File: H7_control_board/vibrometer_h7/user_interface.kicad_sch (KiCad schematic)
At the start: 26 parts, among them J501 Conn_02x08_Odd_Even, J502 Conn_02x08_Odd_Even, SW501 SW_Push, SW502 SW_Push

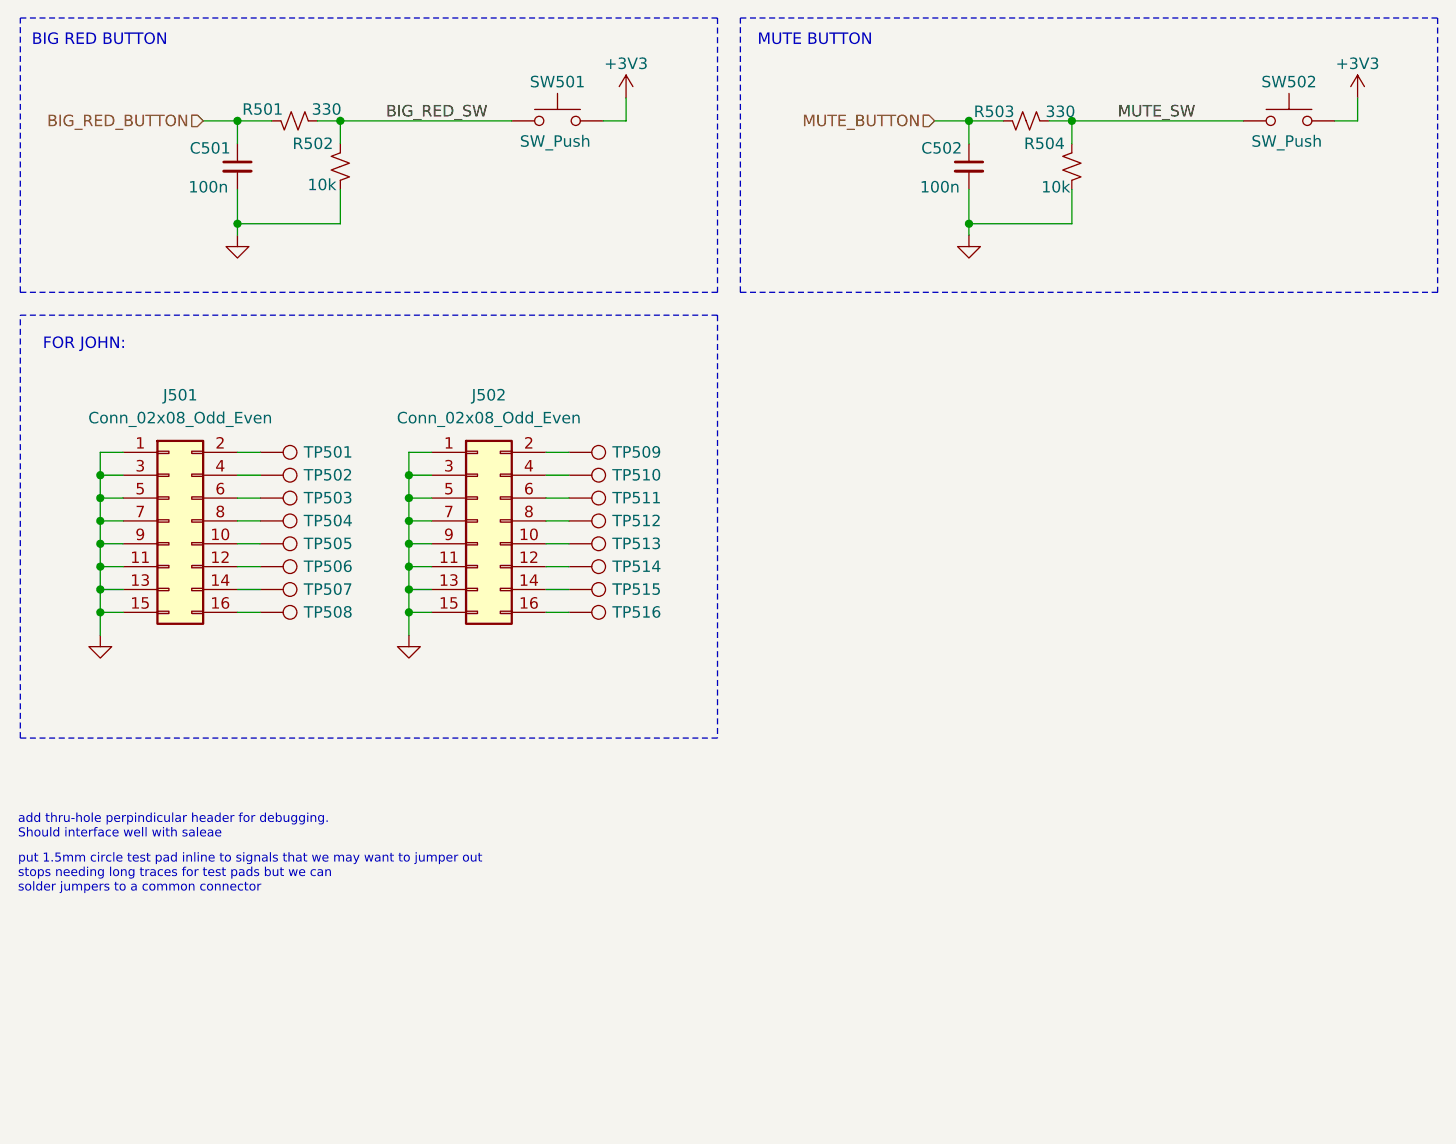
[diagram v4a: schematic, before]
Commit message: added indicator leds
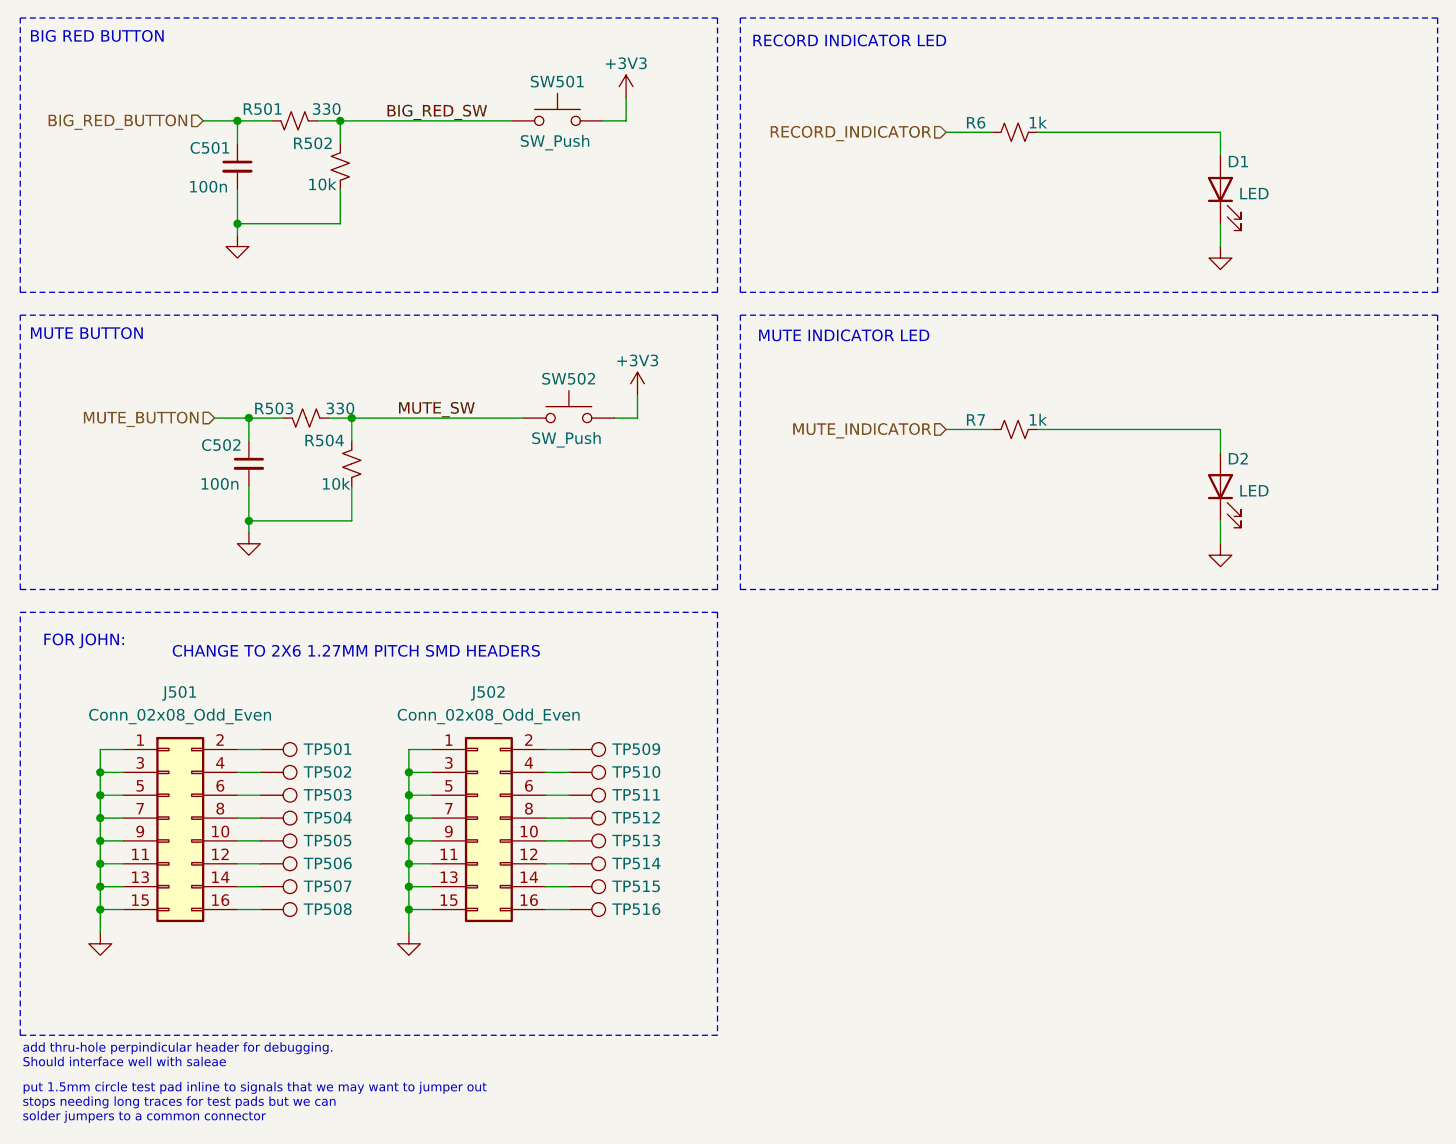
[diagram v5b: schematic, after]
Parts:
- added D1, D2: LED, LED_SMD:LED_0603_1608Metric, symbol Device:LED
- added R6, R7: 1k, Resistor_SMD:R_0603_1608Metric, symbol Device:R_Small_US
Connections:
- net GND: now also D1.1 (K), D2.1 (K)
- new net: D1.2 (A), R6.2
- new net: D2.2 (A), R7.2
- new net MUTE_INDICATOR: R7.1
- new net RECORD_INDICATOR: R6.1
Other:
- note added: "CHANGE TO 2X6 1.27MM PITCH SMD HEADERS"
- note added: "MUTE INDICATOR LED"
- note added: "RECORD INDICATOR LED"
- moved on the sheet: J501, J502, TP501, TP502, TP503, TP504, TP505, TP506, TP507, TP508, TP509, TP510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

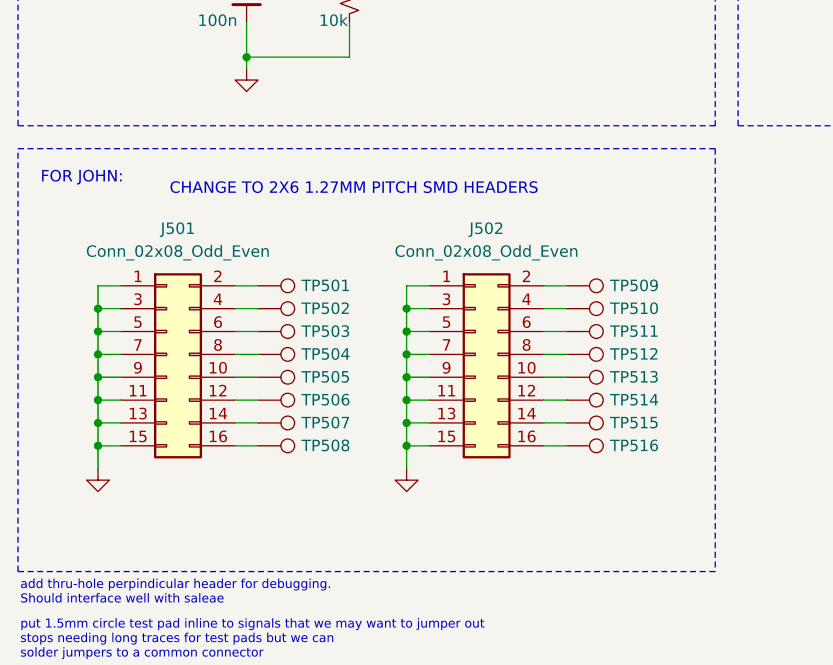
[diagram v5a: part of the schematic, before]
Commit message: connectors, they are so BIG whyyyy john, whyyy
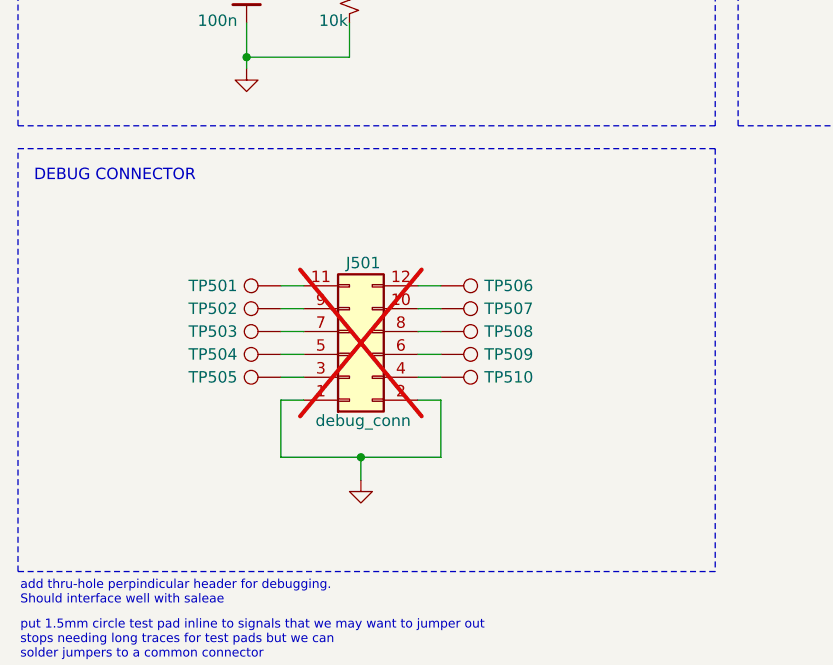
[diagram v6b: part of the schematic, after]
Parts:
- removed J501, J502: Conn_02x08_Odd_Even, Connector_PinHeader_1.00mm:PinHeader_2x08_P1.00mm_Vertical_SMD, symbol Connector_Generic:Conn_02x08_Odd_Even
- removed TP511, TP512, TP513, TP514, TP515, TP516: TestPoint, TestPoint:TestPoint_Pad_D1.0mm, symbol Connector:TestPoint
- added J501: debug_conn, Connector_PinHeader_2.54mm:PinHeader_2x06_P2.54mm_Vertical_SMD, symbol Connector_Generic:Conn_02x06_Odd_Even
- R502, R504: footprint Resistor_SMD:R_0603_1608Metric -> Resistor_SMD:R_0402_1005Metric
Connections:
- net GND: now also J501.1 (Pin_1), J501.2 (Pin_2)
- net at TP504.1: now also J501.5 (Pin_5)
- net at TP507.1: now also J501.10 (Pin_10)
- net at TP505.1: now also J501.3 (Pin_3)
- net at TP506.1: now also J501.12 (Pin_12)
- net at TP508.1: now also J501.8 (Pin_8)
- net at TP501.1: now also J501.11 (Pin_11)
- net at TP502.1: now also J501.9 (Pin_9)
- net at TP503.1: now also J501.7 (Pin_7)
- net at TP509.1: now also J501.6 (Pin_6)
- net at TP510.1: now also J501.4 (Pin_4)
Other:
- note added: "DEBUG CONNECTOR"
- note removed: "CHANGE TO 2X6 1.27MM PITCH SMD HEADERS"
- note removed: "FOR JOHN:"

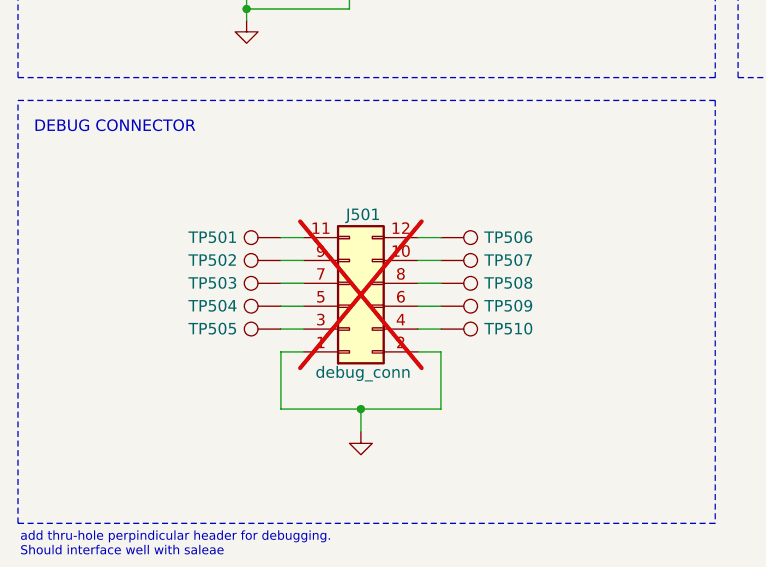
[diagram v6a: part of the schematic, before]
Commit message: some rerouting, cleaned up silkscreen
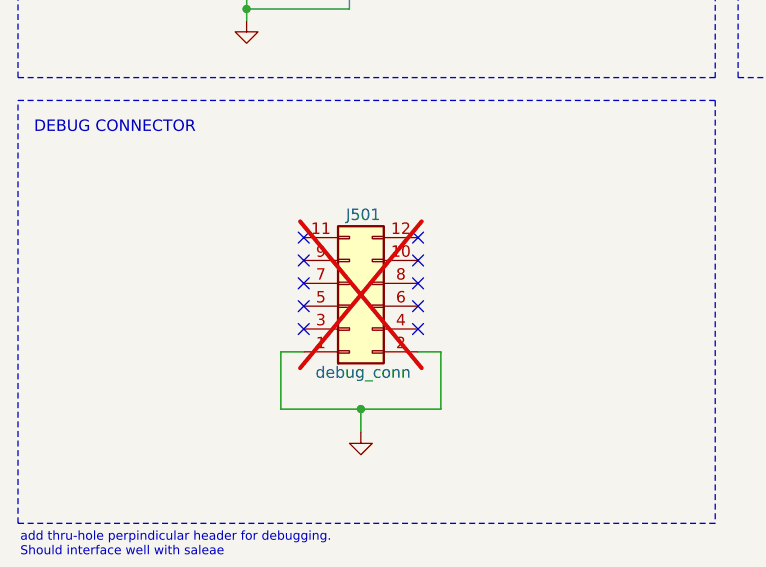
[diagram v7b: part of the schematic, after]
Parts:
- removed TP501, TP502, TP503, TP504, TP505, TP506, TP507, TP508, TP509, TP510: TestPoint, TestPoint:TestPoint_Pad_D1.0mm, symbol Connector:TestPoint
- R6, R7: footprint Resistor_SMD:R_0603_1608Metric -> Resistor_SMD:R_0402_1005Metric; LCSC C21190 -> (none)
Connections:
- no-connect marks 0 -> 10

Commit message: nearly done....
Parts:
- C501, C502: footprint Capacitor_SMD:C_0402_1005Metric_Pad0.74x0.62mm_HandSolder -> Capacitor_SMD:C_0402_1005Metric
- D501: renamed from D1; value LED -> LED_RED; LCSC C965805 -> C965799
- D502: renamed from D2; value LED -> LED_RED; LCSC C965805 -> C965799
- R502: renamed from R6; LCSC (none) -> C11702
- R505: renamed from R7; LCSC (none) -> C11702
- renumbered R502 to R503, R503 to R504, R504 to R506
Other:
- note removed: "add thru-hole perpindicular header for debugging. Should interface well with saleae"
- note removed: "put 1.5mm circle test pad inline to signals that we may want to jumper out stops needing long traces for test pads but we can solder jumpers to a common connector"
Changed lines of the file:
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@@
-		)
-	)
-	(text "add thru-hole perpindicular header for debugging. \nShould interface well with saleae"
-		(exclude_from_sim no)
-		(at 63.754 178.943 0)
-		(effects
-			(font
-				(size 1 1)
-			)
-			(justify left)
 		)
 	)
@@
 			(font
 				(size 1.27 1.27)
-			)
-			(justify left)
-		)
-	)
-	(text "put 1.5mm circle test pad inline to signals that we may want to jumper out\nstops needing long traces for test pads but we can\nsolder jumpers to a common connector"
-		(exclude_from_sim no)
-		(at 63.754 184.15 0)
-		(effects
-			(font
-				(size 1 1)
 			)
 			(justify left)
@@
 		(dnp no)
 		(fields_autoplaced yes)
-		(property "Reference" "#PWR04"
+		(property "Reference" "#PWR0503"
 			(at 196.85 95.25 0)
 			(effects
@@
 			(project "vibrometer_h7"
 				(path "/18de6987-156a-4b34-871e-cbbe1d261986/1264eea6-2da0-4b8c-9a4c-9121bcc9c76c"
-					(reference "#PWR04")
+					(reference "#PWR0503")
 					(unit 1)
 				)
@@
 		(on_board yes)
 		(dnp no)
-		(property "Reference" "R6"
+		(property "Reference" "R502"
 			(at 169.672 75.184 90)
 			(effects
@@
 			)
 		)
-		(property "Datasheet" ""
+		(property "Datasheet" "https://wmsc.lcsc.com/wmsc/upload/file/pdf/v2/lcsc/2206010216_UNI-ROYAL-Uniroyal-Elec-0402WGF1001TCE_C11702.pdf"
 			(at 173.99 76.2 0)
 			(effects
@@
 			)
 		)
-		(property "LCSC" ""
+		(property "LCSC" "C11702"
 			(at 173.99 76.2 0)
 			(effects
@@
 			(project "vibrometer_h7"
 				(path "/18de6987-156a-4b34-871e-cbbe1d261986/1264eea6-2da0-4b8c-9a4c-9121bcc9c76c"
-					(reference "R6")
+					(reference "R502")
 					(unit 1)
 				)
@@
 		(on_board yes)
 		(dnp no)
-		(property "Reference" "#PWR0503"
+		(property "Reference" "#PWR0501"
 			(at 130.81 76.2 0)
 			(effects
@@
 			(project "vibrometer_h7"
 				(path "/18de6987-156a-4b34-871e-cbbe1d261986/1264eea6-2da0-4b8c-9a4c-9121bcc9c76c"
-					(reference "#PWR0503")
+					(reference "#PWR0501")
 					(unit 1)
 				)
@@
 		(on_board yes)
 		(dnp no)
-		(property "Reference" "#PWR0502"
+		(property "Reference" "#PWR0507"
 			(at 101.6 172.72 0)
 			(effects
@@
 			(project "vibrometer_h7"
 				(path "/18de6987-156a-4b34-871e-cbbe1d261986/1264eea6-2da0-4b8c-9a4c-9121bcc9c76c"
-					(reference "#PWR0502")
+					(reference "#PWR0507")
 					(unit 1)
 				)
@@
 		(on_board yes)
 		(dnp no)
-		(property "Reference" "D1"
+		(property "Reference" "D501"
 			(at 197.612 79.502 90)
 			(effects
@@
 			)
 		)
-		(property "Value" "LED"
+		(property "Value" "LED_RED"
 			(at 198.882 83.058 90)
 			(effects
@@
 			)
 		)
-		(property "LCSC" "C965805"
+		(property "LCSC" "C965799"
 			(at 196.85 82.55 0)
 			(effects
@@
 			(project "vibrometer_h7"
 				(path "/18de6987-156a-4b34-871e-cbbe1d261986/1264eea6-2da0-4b8c-9a4c-9121bcc9c76c"
-					(reference "D1")
+					(reference "D501")
 					(unit 1)
 				)
@@
 		(on_board yes)
 		(dnp no)
-		(property "Reference" "#PWR0501"
+		(property "Reference" "#PWR0502"
 			(at 87.63 93.98 0)
 			(effects
@@
 			(project "vibrometer_h7"
 				(path "/18de6987-156a-4b34-871e-cbbe1d261986/1264eea6-2da0-4b8c-9a4c-9121bcc9c76c"
-					(reference "#PWR0501")
+					(reference "#PWR0502")
 					(unit 1)
 				)
@@
 		(on_board yes)
 		(dnp no)
-		(property "Reference" "R504"
+		(property "Reference" "R506"
 			(at 97.282 110.49 0)
 			(effects
@@
 			(project "vibrometer_h7"
 				(path "/18de6987-156a-4b34-871e-cbbe1d261986/1264eea6-2da0-4b8c-9a4c-9121bcc9c76c"
-					(reference "R504")
+					(reference "R506")
 					(unit 1)
 				)
@@
 		(on_board yes)
 		(dnp no)
-		(property "Reference" "#PWR02"
+		(property "Reference" "#PWR0504"
 			(at 132.08 109.22 0)
 			(effects
@@
 			(project "vibrometer_h7"
 				(path "/18de6987-156a-4b34-871e-cbbe1d261986/1264eea6-2da0-4b8c-9a4c-9121bcc9c76c"
-					(reference "#PWR02")
+					(reference "#PWR0504")
 					(unit 1)
 				)
@@
 			)
 		)
-		(property "Footprint" "Capacitor_SMD:C_0402_1005Metric_Pad0.74x0.62mm_HandSolder"
+		(property "Footprint" "Capacitor_SMD:C_0402_1005Metric"
 			(at 88.9 113.03 0)
 			(effects
@@
 		(on_board yes)
 		(dnp no)
-		(property "Reference" "D2"
+		(property "Reference" "D502"
 			(at 197.612 112.522 90)
 			(effects
@@
 			)
 		)
-		(property "Value" "LED"
+		(property "Value" "LED_RED"
 			(at 198.882 116.078 90)
 			(effects
@@
 			)
 		)
-		(property "LCSC" "C965805"
+		(property "LCSC" "C965799"
 			(at 196.85 115.57 0)
 			(effects
@@
 			(project "vibrometer_h7"
 				(path "/18de6987-156a-4b34-871e-cbbe1d261986/1264eea6-2da0-4b8c-9a4c-9121bcc9c76c"
-					(reference "D2")
+					(reference "D502")
 					(unit 1)
 				)
@@
 		(on_board yes)
 		(dnp no)
-		(property "Reference" "R502"
+		(property "Reference" "R503"
 			(at 96.012 77.47 0)
 			(effects
@@
 			(project "vibrometer_h7"
 				(path "/18de6987-156a-4b34-871e-cbbe1d261986/1264eea6-2da0-4b8c-9a4c-9121bcc9c76c"
-					(reference "R502")
+					(reference "R503")
 					(unit 1)
 				)
@@
 		(on_board yes)
 		(dnp no)
-		(property "Reference" "R503"
+		(property "Reference" "R504"
 			(at 91.694 106.934 90)
 			(effects
@@
 			(project "vibrometer_h7"
 				(path "/18de6987-156a-4b34-871e-cbbe1d261986/1264eea6-2da0-4b8c-9a4c-9121bcc9c76c"
-					(reference "R503")
+					(reference "R504")
 					(unit 1)
 				)
@@
 		(on_board yes)
 		(dnp no)
-		(property "Reference" "#PWR01"
+		(property "Reference" "#PWR0505"
 			(at 88.9 127 0)
 			(effects
@@
 			(project "vibrometer_h7"
 				(path "/18de6987-156a-4b34-871e-cbbe1d261986/1264eea6-2da0-4b8c-9a4c-9121bcc9c76c"
-					(reference "#PWR01")
+					(reference "#PWR0505")
 					(unit 1)
 				)
@@
 		(dnp no)
 		(fields_autoplaced yes)
-		(property "Reference" "#PWR06"
+		(property "Reference" "#PWR0506"
 			(at 196.85 128.27 0)
 			(effects
@@
 			(project "vibrometer_h7"
 				(path "/18de6987-156a-4b34-871e-cbbe1d261986/1264eea6-2da0-4b8c-9a4c-9121bcc9c76c"
-					(reference "#PWR06")
+					(reference "#PWR0506")
 					(unit 1)
 				)
@@
 		(on_board yes)
 		(dnp no)
-		(property "Reference" "R7"
+		(property "Reference" "R505"
 			(at 169.672 108.204 90)
 			(effects
@@
 			)
 		)
-		(property "Datasheet" ""
+		(property "Datasheet" "https://wmsc.lcsc.com/wmsc/upload/file/pdf/v2/lcsc/2206010216_UNI-ROYAL-Uniroyal-Elec-0402WGF1001TCE_C11702.pdf"
 			(at 173.99 109.22 0)
 			(effects
@@
 			)
 		)
-		(property "LCSC" ""
+		(property "LCSC" "C11702"
 			(at 173.99 109.22 0)
 			(effects
@@
 			(project "vibrometer_h7"
 				(path "/18de6987-156a-4b34-871e-cbbe1d261986/1264eea6-2da0-4b8c-9a4c-9121bcc9c76c"
-					(reference "R7")
+					(reference "R505")
 					(unit 1)
 				)
@@
 			)
 		)
-		(property "Footprint" "Capacitor_SMD:C_0402_1005Metric_Pad0.74x0.62mm_HandSolder"
+		(property "Footprint" "Capacitor_SMD:C_0402_1005Metric"
 			(at 87.63 80.01 0)
 			(effects
